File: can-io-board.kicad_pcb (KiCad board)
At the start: 2 copper layers, 30 x 15.8 mm, 23 parts, among them J1 Conn_02x13_Odd_Even, U1 STM32F302K8U6, U2 MCP1703, U3 MAX3051, X1 16MHz 10ppm

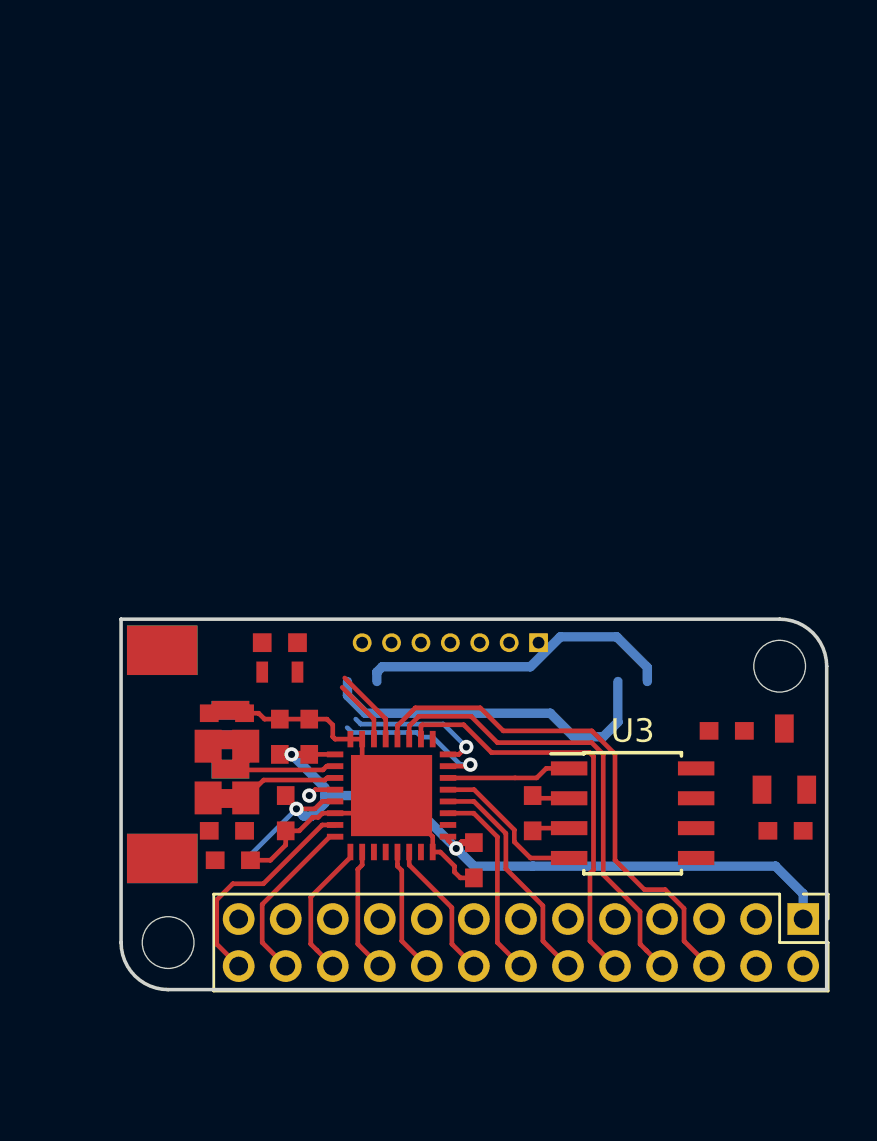
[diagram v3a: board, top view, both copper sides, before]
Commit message: Reduced number of IO, use PicoBlade connector
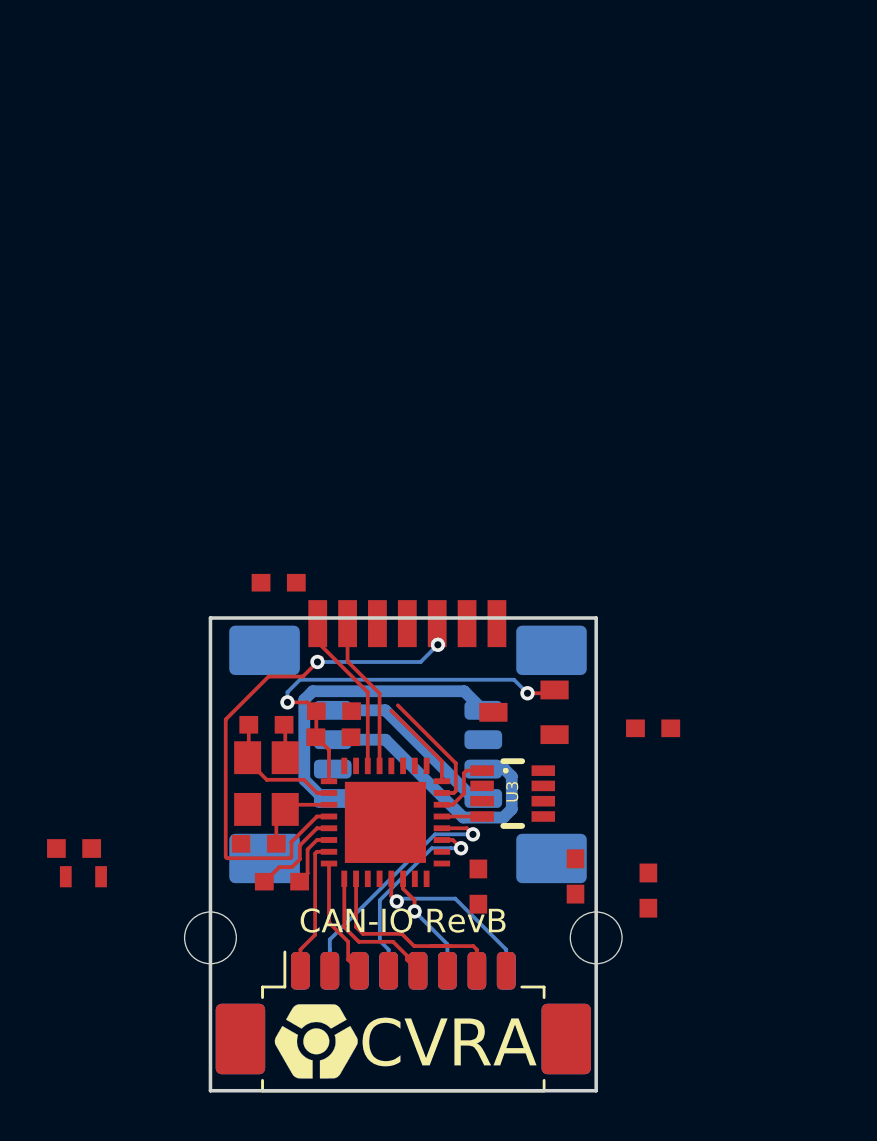
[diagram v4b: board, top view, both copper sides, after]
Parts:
- added J2: CONN_PWM, Connector_Molex:Molex_PicoBlade_53261-0871_1x08-1MP_P1.25mm_Horizontal, F.Cu at (92.0, 81.6)
- CONN1: footprint Connectors_Molex:Connector_Molex_PicoBlade_53047-0710 -> _connectors:_Solder_Pad1.27_7
- CONN2: footprint Connectors_Molex:Connector_Molex_PicoBlade_53261-0471 -> Connector_Molex:Molex_PicoBlade_53261-0471_1x04-1MP_P1.25mm_Horizontal; moved to B.Cu
- CONN3: footprint Connectors_Molex:Connector_Molex_PicoBlade_53261-0471 -> Connector_Molex:Molex_PicoBlade_53261-0471_1x04-1MP_P1.25mm_Horizontal
- G***: moved to F.Cu
- J1: value Conn_02x13_Odd_Even -> CONN_IO; footprint Connector_PinHeader_2.00mm:PinHeader_2x13_P2.00mm_Vertical -> Connector_Molex:Molex_PicoBlade_53261-0871_1x08-1MP_P1.25mm_Horizontal; moved to B.Cu
- U3: footprint Package_SO:SOIC-8_3.9x4.9mm_P1.27mm -> _std:_SOT23-8
- moved G*** 23.3 mm to (88.3, 82.2), turned to 0 degrees
- moved J1 17.6 mm to (92.0, 81.6), turned to 180 degrees
- moved CONN2 16.0 mm to (97.8, 70.0)
- moved H2 13.9 mm to (100.2, 77.8)
- moved D1 12.4 mm to (78.0, 74.0)
- moved R1 12.1 mm to (78.4, 75.2)
- moved C4 12.0 mm to (86.7, 62.7)
- moved U2 9.13 mm to (98.4, 69.2), turned to 90 degrees
- moved C9 7.56 mm to (102.4, 75.8), turned to 270 degrees
- moved C10 7.12 mm to (102.6, 68.9), turned to 0 degrees
- moved U3 6.65 mm to (95.3, 70.7), turned to 270 degrees
- moved CONN1 5.64 mm to (92.2, 64.4)
- moved CONN3 4.85 mm to (86.6, 70.0)
- moved C8 3.25 mm to (99.3, 75.2), turned to 270 degrees
- moved C3 2.91 mm to (86.8, 75.4), turned to 0 degrees
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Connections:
- J1 pad 1: VCC -> /PWM0_PA6_TIM16_CH1
- J1 pad 2: VCC -> GND
- J1 pad 3: /5V_CAN -> /PWM1_PA7_TIM17_CH1
- J1 pad 4: /5V_CAN -> GND
- J1 pad 5: GND -> /PWM2_PA9_TIM1_CH2
- J1 pad 6: /IO_PB5_SPI3MOSI -> GND
- J1 pad 7: GND -> /PWM3_PA10_TIM1_CH3
- J1 pad 8: /IO_PB4_SPI3MISO_UART2RX -> GND
- U1 pad 10: /IO_PA3_TIM2CH4_UART2_RX_ADC4 -> /IO3_PA3
- U1 pad 13: /IO_PA6_TIM16CH1_ADC10 -> /PWM0_PA6_TIM16_CH1
- U1 pad 14: /IO_PA7_TIM17CH1_ADC15 -> /PWM1_PA7_TIM17_CH1
- U1 pad 19: /IO_PA9_I2C2SCL_UART1TX -> /PWM2_PA9_TIM1_CH2
- U1 pad 20: /IO_PA10_I2C2SDA_UART1RX -> /PWM3_PA10_TIM1_CH3
- U1 pad 26: /IO_PB3_SPI3SCK_UART2TX -> (no net)
- U1 pad 27: /IO_PB4_SPI3MISO_UART2RX -> (no net)
- U1 pad 28: /IO_PB5_SPI3MOSI -> (no net)
- U1 pad 7: /IO_PA0_TIM2CH1_UART2_CTS_ADC1 -> /IO0_PA0
- U1 pad 8: /IO_PA1_TIM2CH2_UART2_RTS_ADC2 -> /IO1_PA1
- U1 pad 9: /IO_PA2_TIM2CH3_UART2_TX_ADC3 -> /IO2_PA2
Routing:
- net /IO_PB5_SPI3MOSI: track 22.1 -> 0.00 mm
- net /RST: track 1.20 -> 22.0 mm, vias 1 -> 2
- net /IO_PB4_SPI3MISO_UART2RX: track 19.7 -> 0.00 mm
- net /IO_PB3_SPI3SCK_UART2TX: track 17.9 -> 0.00 mm
- net VCC: track 38.8 -> 21.0 mm, vias 3 -> 2
- net GND: track 19.7 -> 4.01 mm
- net /5V_CAN: track 0.00 -> 13.0 mm
- net /PWM3_PA10_TIM1_CH3: track 0.00 -> 10.7 mm, vias 0 -> 1
- net /IO_PA10_I2C2SDA_UART1RX: track 9.76 -> 0.00 mm
- net /IO_PA0_TIM2CH1_UART2_CTS_ADC1: track 9.56 -> 0.00 mm
- net /IO3_PA3: track 0.00 -> 9.30 mm
- net /PWM2_PA9_TIM1_CH2: track 0.00 -> 8.48 mm, vias 0 -> 1
- net /IO_PA9_I2C2SCL_UART1TX: track 8.42 -> 0.00 mm
- net /PWM0_PA6_TIM16_CH1: track 0.00 -> 7.56 mm, vias 0 -> 1
- net /IO_PA1_TIM2CH2_UART2_RTS_ADC2: track 7.33 -> 0.00 mm
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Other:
- board size 30 x 15.8 mm -> 16.4 x 20.1 mm
- board text removed: "3.3V"
- board text removed: "5V"
- board text removed: "A0"
- board text removed: "A1"
- board text removed: "A10"
- board text removed: "A2"
- board text removed: "A3"
- board text removed: "A6"
- board text removed: "A7"
- board text removed: "A9"
- board text removed: "B3"
- board text removed: "B4"
- board text removed: "B5"
- board text removed: "GND"

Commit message: Routing almost finished
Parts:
- removed H1, H2: MountingHole M2, MountingHole:MountingHole_2.2mm_M2_DIN965
- C1, C10, C9: footprint Capacitors_SMD:C_0603 -> Capacitor_SMD:C_0603_1608Metric
- C2, C3, C4, C5, C6, C7, C8: footprint Capacitors_SMD:C_0603 -> Capacitor_SMD:C_0402_1005Metric
- D1: footprint LEDs:LED-0603 -> LED_SMD:LED_0603_1608Metric
- G***: moved to B.Cu
- R1: footprint Resistors_SMD:R_0603 -> Resistor_SMD:R_0402_1005Metric
- X1: footprint _div:_TSX-3225-SMD-XTAL -> Crystal:Crystal_SMD_SeikoEpson_TSX3225-4Pin_3.2x2.5mm
- moved D1 18.2 mm to (95.9, 77.1), turned to 180 degrees
- moved R1 15.2 mm to (93.5, 77.1)
- moved C9 12.0 mm to (93.0, 68.3), turned to 90 degrees
- moved G*** 9.18 mm to (92.2, 73.9), turned to 90 degrees
- moved C4 5.50 mm to (86.4, 68.2)
- moved C10 4.14 mm to (98.5, 69.0), turned to 270 degrees
- moved C8 1.66 mm to (97.7, 75.2), turned to 0 degrees
- moved U2 1.61 mm to (97.1, 70.0)
- moved U3 1.32 mm to (95.6, 72.0)
- moved CONN1 1.05 mm to (92.0, 65.5)
- moved C7 0.70 mm to (86.4, 69.4)
- moved C5 0.69 mm to (89.0, 70.0)
- moved U1 0.69 mm to (91.2, 73.6)
- moved C1 0.68 mm to (88.8, 68.8)
- moved X1 0.53 mm to (86.4, 71.7)
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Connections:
- D1 pad 1: Net-(D1-Pad1) -> GND
- D1 pad 2: /LED -> Net-(D1-Pad2)
- R1 pad 1: Net-(D1-Pad1) -> /LED
- R1 pad 2: GND -> Net-(D1-Pad2)
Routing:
- net GND: track 4.01 -> 61.9 mm, vias 0 -> 19
- net VCC: track 21.0 -> 61.8 mm, vias 2 -> 0
- net Net-(CONN2-Pad4): track 7.95 -> 16.2 mm, vias 0 -> 1
- net /SWCK: track 3.89 -> 7.72 mm
- net /SWIO: track 5.29 -> 8.99 mm
- net /LED: track 0.00 -> 3.50 mm
- net /5V_CAN: track 13.0 -> 16.1 mm, vias 0 -> 1
- net Net-(CONN2-Pad3): track 11.9 -> 13.8 mm, vias 0 -> 1
- net /IO3_PA3: track 9.30 -> 7.36 mm
- net Net-(D1-Pad2): track 0.00 -> 1.19 mm
- net /RST: track 22.0 -> 20.9 mm
- net /IO1_PA1: track 5.32 -> 4.41 mm
- net /IO_PB6_I2C1SCL_UART1TX: track 6.54 -> 5.64 mm
- net /IO2_PA2: track 6.06 -> 5.34 mm
- net /IO0_PA0: track 5.86 -> 5.16 mm
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- added copper zone on B.Cu, net GND
- added copper zone on F.Cu, net GND
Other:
- outline, holes or cut-outs redrawn
- board text added: "+"
- board text added: "Designed by: Michael Spieler"
